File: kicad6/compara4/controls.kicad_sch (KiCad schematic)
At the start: 15 parts, among them J10 In_4, J11 CV_Jack, J3 In_1, J4 In_2, J5 In_3, J6 Out_XOR, J7 Out_XNOR, J8 Out_OR, J9 Out_NOR, SW1 SW_SPDT

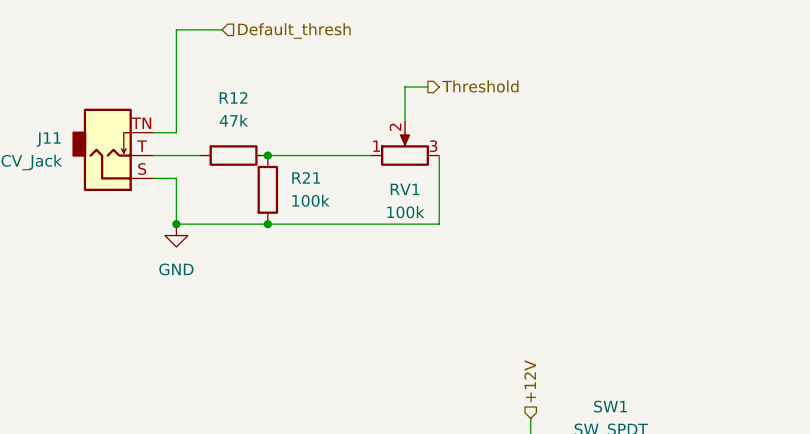
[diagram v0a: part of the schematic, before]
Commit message: compara4: reverse pot and cleanup ERC
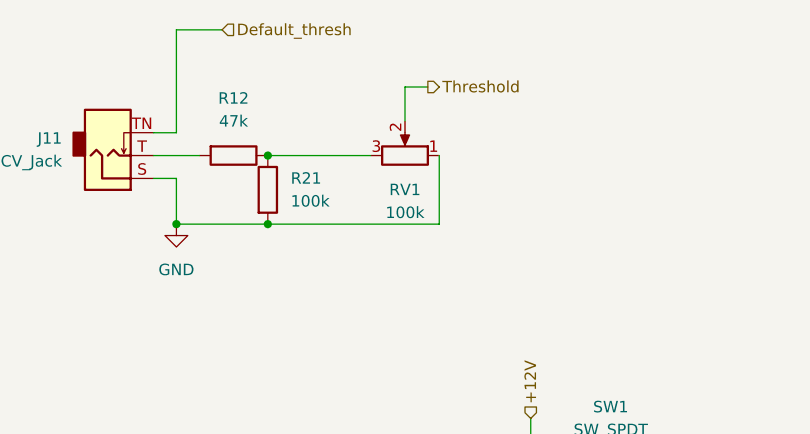
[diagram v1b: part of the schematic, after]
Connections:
- net GND: now also RV1.1; no longer RV1.3
- net at R12.1, R21.1: now also RV1.3; no longer RV1.1
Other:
- moved on the sheet: RV1
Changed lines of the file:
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@@
     (pin "TN")
   )
-  (symbol (lib_id "Device:R_Potentiometer") (at 104.14 48.26 90) (unit 1)
+  (symbol (lib_id "Device:R_Potentiometer") (at 104.14 48.26 270) (mirror x) (unit 1)
     (in_bom yes) (on_board yes) (fields_autoplaced)
     (property "Reference" "RV1" (id 0) (at 104.14 52.07 90))
